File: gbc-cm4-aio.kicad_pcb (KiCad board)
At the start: 4 copper layers, 70.1 x 122.2 mm, 130 parts, among them J1 Conn_01x40, J2 AudioJack2_Ground_Switch, J4 DM3D-SF, J6 Conn_01x11, J7 Conn_01x02, P1 USB_C_Plug_USB2.0, Q1 AO4407C, Q3 2N7002E, SW1 SW_Push, SW3 SW_Push_Dual_x2, SW4 SW_SPDT, U1 SGM2019-2.8YN5G/TR, U10 TPS61022RWUR, U2 FAN5333B, U3 RT9742GGJ5, U4 MAX17048G, U5 PCM5102, U6 PAM8302AAY, U7 SGM3204YN6G/TR, U9 MCP73871-2CAI_ML

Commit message: battery connector positioning improvement
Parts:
- moved C36 8.97 mm to (195.1, 230.3), turned to 0 degrees
- moved J7 2.25 mm to (198.0, 226.4), turned to 0 degrees
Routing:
- net +BATT: track 60.8 -> 54.5 mm

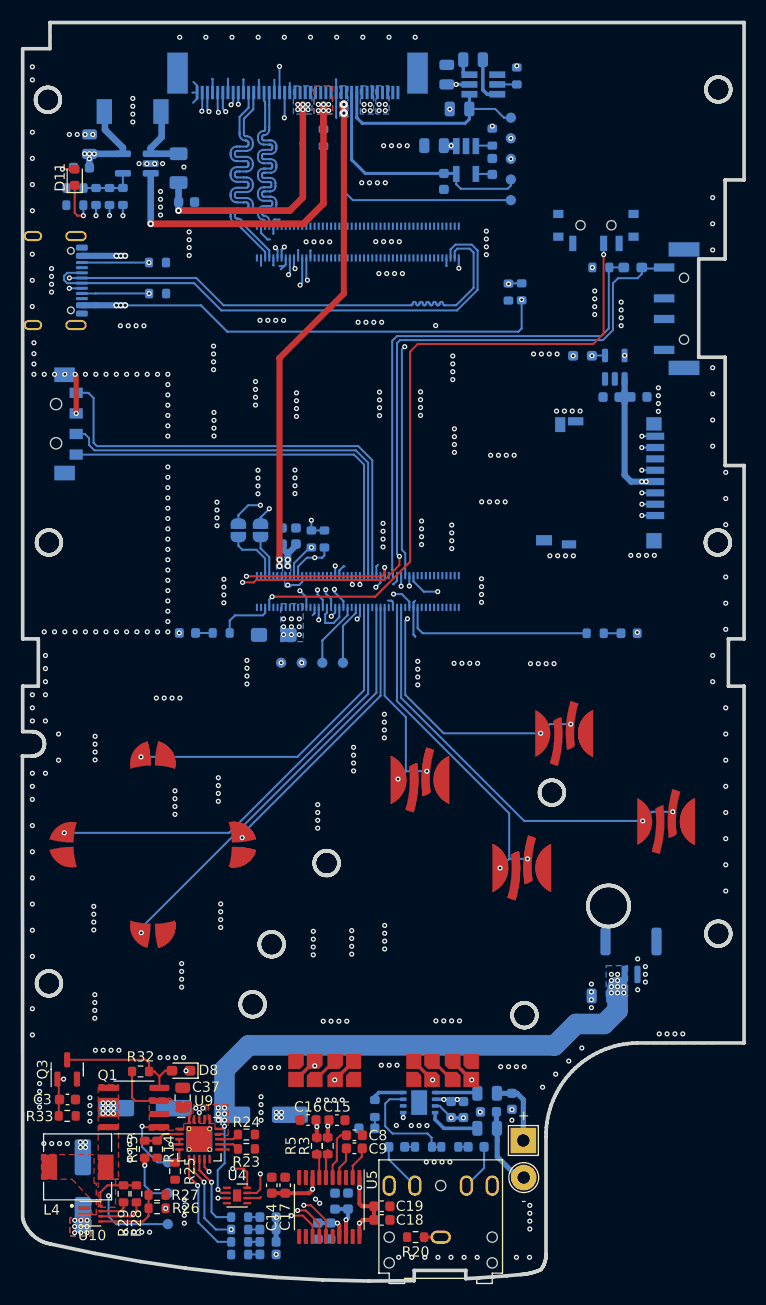
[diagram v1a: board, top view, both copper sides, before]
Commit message: relayout power supply and audio
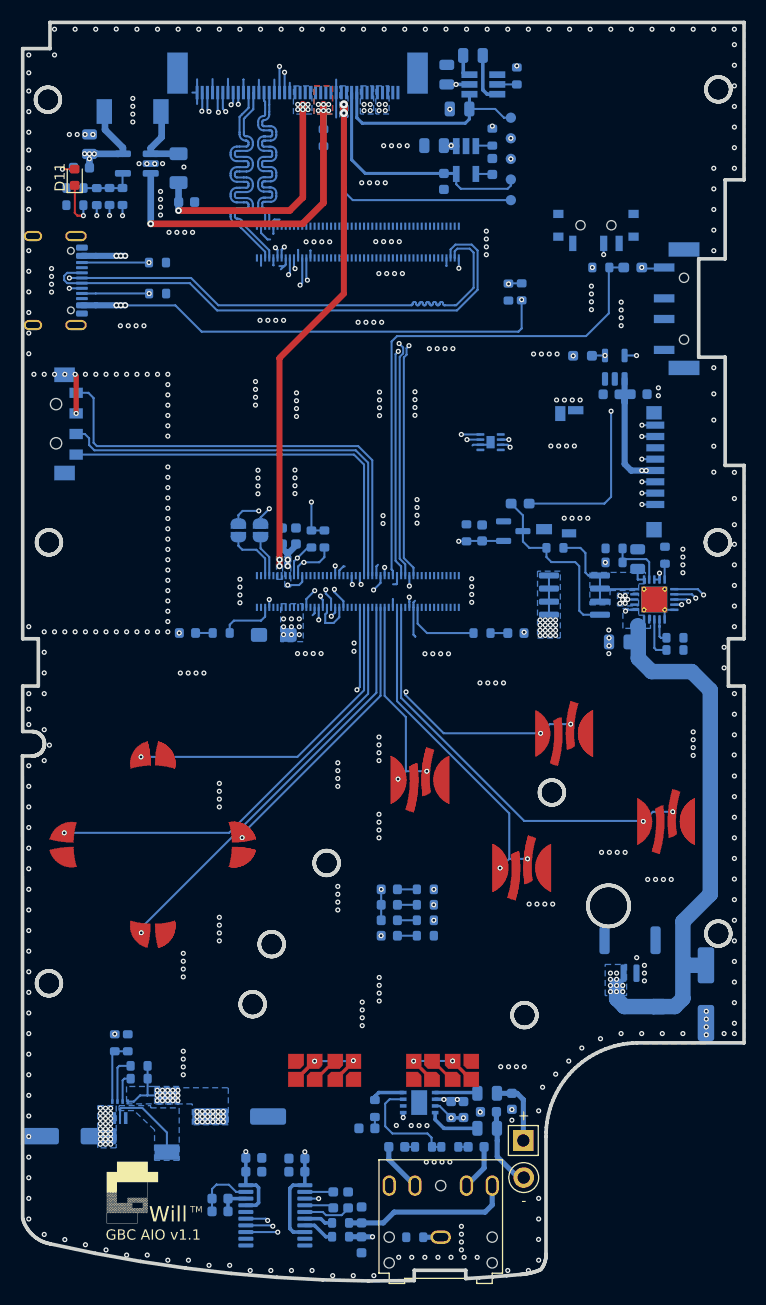
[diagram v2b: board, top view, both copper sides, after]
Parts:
- removed C18: 10uF, Capacitor_SMD:C_0603_1608Metric
- removed C19: 0.1uF, Capacitor_SMD:C_0603_1608Metric
- removed RX1: RX, TestPoint:TestPoint_Pad_D1.0mm
- removed SCL1: SCL, TestPoint:TestPoint_Pad_D1.0mm
- removed SDA1: SDA, TestPoint:TestPoint_Pad_D1.0mm
- removed TX1: TX, TestPoint:TestPoint_Pad_D1.0mm
- removed VBAT1: VBAT, TestPoint:TestPoint_Pad_D1.0mm
- removed VBUS1: VBUS, TestPoint:TestPoint_Pad_D1.0mm
- removed VIN1: VIN, TestPoint:TestPoint_Pad_D1.0mm
- added ?: , LOGO, F.Cu at (148.6, 250.4)
- C14, C15, C16, C17, C3, C37, C8, C9, D8, L4, Q1, Q3, R14, R15, R20, R23, R24, R25, R26, R27, R28, R29, R3, R32, R33, R5, U10, U4, U5, U9: moved to B.Cu
- moved U4 77.2 mm to (184.3, 176.6), turned to 180 degrees
- moved R25 76.4 mm to (201.3, 187.6), turned to 90 degrees
- moved R14 73.3 mm to (196.3, 186.9), turned to 180 degrees
- moved R15 72.9 mm to (196.3, 188.3), turned to 0 degrees
- moved R33 68.6 mm to (182.0, 185.4), turned to -90 degrees
- moved U9 68.5 mm to (200.2, 191.9), turned to -90 degrees
- moved C37 68.4 mm to (198.6, 187.9)
- moved C3 68.2 mm to (183.5, 185.4), turned to -90 degrees
- moved Q3 67.9 mm to (186.5, 185.2), turned to 0 degrees
- moved Q1 65.6 mm to (192.5, 191.4)
- moved R32 64.8 mm to (190.6, 186.8), turned to 180 degrees
- moved R23 64.8 mm to (202.2, 195.6)
- moved D8 64.1 mm to (187.2, 182.6)
- moved R24 62.8 mm to (202.2, 196.8)
- moved C39 44.7 mm to (205.2, 230.2), turned to -90 degrees
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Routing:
- net Net-(D8-K): track 141.0 -> 34.8 mm, vias 3 -> 2
- net /VIN: track 13.2 -> 88.9 mm, vias 10 -> 49
- net /PWR_ON: track 83.6 -> 14.6 mm, vias 3 -> 2
- net Net-(U9-~{PG}): track 10.5 -> 57.9 mm, vias 1 -> 2
- net Net-(U9-STAT2): track 9.20 -> 55.9 mm
- net /SDA0: track 75.1 -> 28.8 mm, vias 3 -> 2
- net Net-(U9-STAT1/~{LBO}): track 7.76 -> 53.9 mm, vias 1 -> 2
- net /SCL0: track 71.4 -> 29.3 mm, vias 3 -> 2
- net VBUS: track 181.7 -> 209.7 mm, vias 14 -> 17
- net +BATT: track 54.5 -> 82.4 mm, vias 18 -> 12
- net /DSI1_RESET: track 66.6 -> 89.5 mm
- net /ACT_LED: track 18.7 -> 7.39 mm
- net /BL_EN: track 67.4 -> 58.0 mm, vias 3 -> 2
- net GND: track 45.0 -> 53.5 mm, vias 463 -> 459
- net /SW: track 0.00 -> 8.21 mm
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- added copper zone on B.Cu, net /SW
- added copper zone on B.Cu, net /VBAT
- added copper zone on B.Cu, net /VIN
- added copper zone on In2.Cu, net /VIN
- added copper zone on B.Cu, net VBUS
- removed copper zone on F.Cu, net +5V
- removed copper zone on F.Cu, net +BATT
- removed copper zone on F.Cu, net /SW
- removed copper zone on F.Cu, net /VBAT
- removed copper zone on F.Cu, net /VIN
- removed copper zone on F.Cu, net VBUS
